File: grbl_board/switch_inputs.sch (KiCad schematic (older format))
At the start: 19 parts

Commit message: spindle control stage
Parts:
- added J?: PROBE, symbol Connector:Screw_Terminal_01x02
- added R?: 1k, symbol Device:R
- added U?: 6N137, Package_DIP:DIP-8_W7.62mm, symbol Isolator:6N137
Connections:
- net +12V: now also J?.1 (Pin_1)
- net +5V: now also U?.7 (EN), U?.8 (VCC)
- net GND: now also U?.3 (C), U?.5 (GND)
- new net: R?.1, U?.2 (A)
- new net: J?.2 (Pin_2), R?.2
- new net PROBE: U?.6 (VO)
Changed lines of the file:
@@
 Wire Wire Line
 	6600 5350 6900 5350
+$Comp
+L Isolator:6N137 U?
+U 1 1 6269851C
+P 3500 6900
+F 0 "U?" H 3500 7367 50  0000 C CNN
+F 1 "6N137" H 3500 7276 50  0000 C CNN
+F 2 "Package_DIP:DIP-8_W7.62mm" H 3500 6400 50  0001 C CNN
+F 3 "https://docs.broadcom.com/docs/AV02-0940EN" H 2650 7450 50  0001 C CNN
+	1    3500 6900
+	1    0    0    -1
+$EndComp
+$Comp
+L power:+5V #PWR?
+U 1 1 62698522
+P 4000 6500
+F 0 "#PWR?" H 4000 6350 50  0001 C CNN
+F 1 "+5V" H 4015 6673 50  0000 C CNN
+F 2 "" H 4000 6500 50  0001 C CNN
+F 3 "" H 4000 6500 50  0001 C CNN
+	1    4000 6500
+	1    0    0    -1
+$EndComp
+Wire Wire Line
+	4000 6500 4000 6700
+Wire Wire Line
+	4000 6700 3800 6700
+Wire Wire Line
+	4000 6700 4000 6800
+Wire Wire Line
+	4000 6800 3800 6800
+Connection ~ 4000 6700
+$Comp
+L power:GND #PWR?
+U 1 1 6269852D
+P 4000 7150
+F 0 "#PWR?" H 4000 6900 50  0001 C CNN
+F 1 "GND" H 4005 6977 50  0000 C CNN
+F 2 "" H 4000 7150 50  0001 C CNN
+F 3 "" H 4000 7150 50  0001 C CNN
+	1    4000 7150
+	1    0    0    -1
+$EndComp
+Wire Wire Line
+	4000 7150 4000 7100
+Wire Wire Line
+	4000 7100 3800 7100
+$Comp
+L Device:R R?
+U 1 1 62698535
+P 2750 6900
+F 0 "R?" V 2543 6900 50  0000 C CNN
+F 1 "1k" V 2634 6900 50  0000 C CNN
+F 2 "" V 2680 6900 50  0001 C CNN
+F 3 "~" H 2750 6900 50  0001 C CNN
+	1    2750 6900
+	0    1    1    0
+$EndComp
+$Comp
+L power:GND #PWR?
+U 1 1 6269853B
+P 3000 7150
+F 0 "#PWR?" H 3000 6900 50  0001 C CNN
+F 1 "GND" H 3005 6977 50  0000 C CNN
+F 2 "" H 3000 7150 50  0001 C CNN
+F 3 "" H 3000 7150 50  0001 C CNN
+	1    3000 7150
+	1    0    0    -1
+$EndComp
+Wire Wire Line
+	3200 7100 3000 7100
+Wire Wire Line
+	3000 7100 3000 7150
+Wire Wire Line
+	2900 6900 3200 6900
+Text HLabel 4000 6900 2    50   Input ~ 0
+PROBE
+Wire Wire Line
+	4000 6900 3800 6900
+$Comp
+L Connector:Screw_Terminal_01x02 J?
+U 1 1 62698546
+P 1400 7000
+F 0 "J?" H 1318 6675 50  0000 C CNN
+F 1 "PROBE" H 1318 6766 50  0000 C CNN
+F 2 "" H 1400 7000 50  0001 C CNN
+F 3 "~" H 1400 7000 50  0001 C CNN
+	1    1400 7000
+	-1   0    0    1
+$EndComp
+Wire Wire Line
+	1600 6900 2600 6900
+$Comp
+L power:+12V #PWR?
+U 1 1 6269854D
+P 1800 6700
+F 0 "#PWR?" H 1800 6550 50  0001 C CNN
+F 1 "+12V" H 1815 6873 50  0000 C CNN
+F 2 "" H 1800 6700 50  0001 C CNN
+F 3 "" H 1800 6700 50  0001 C CNN
+	1    1800 6700
+	1    0    0    -1
+$EndComp
+Wire Wire Line
+	1800 6700 1800 7000
+Wire Wire Line
+	1800 7000 1600 7000
 $EndSCHEMATC

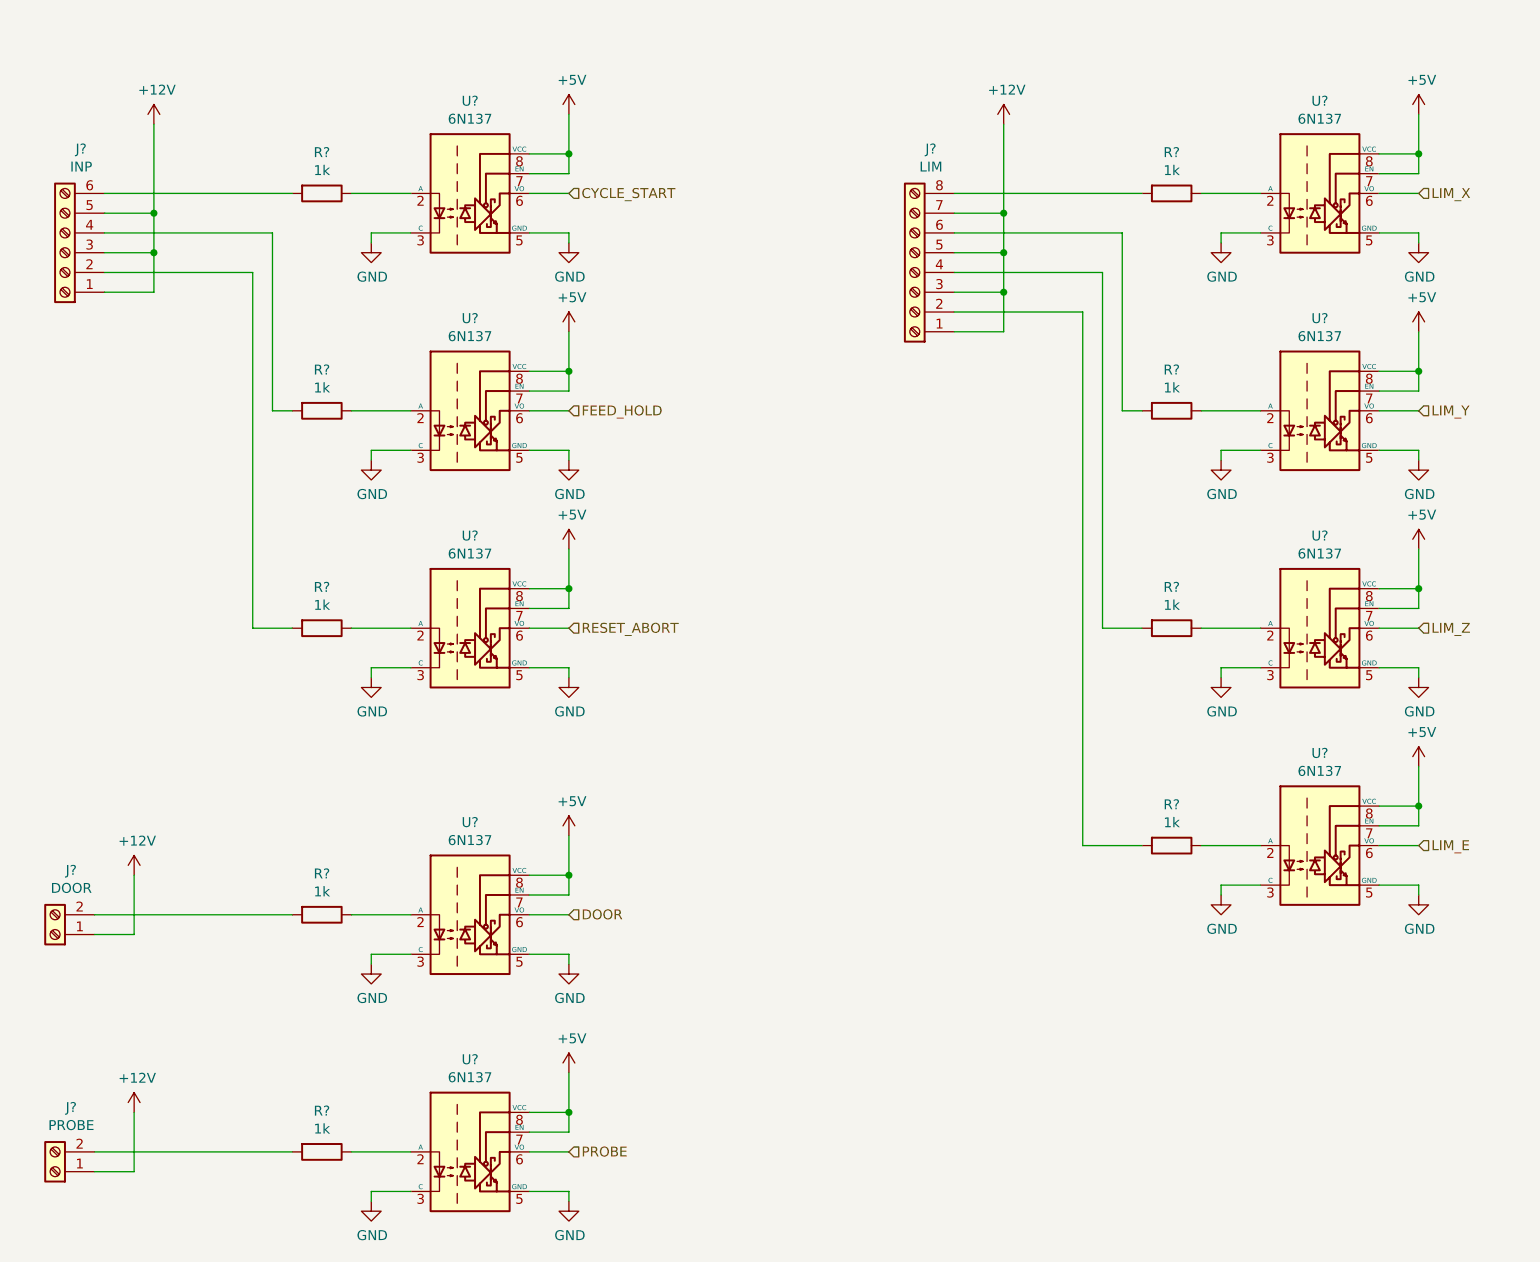
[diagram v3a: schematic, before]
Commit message: added some footprint associations
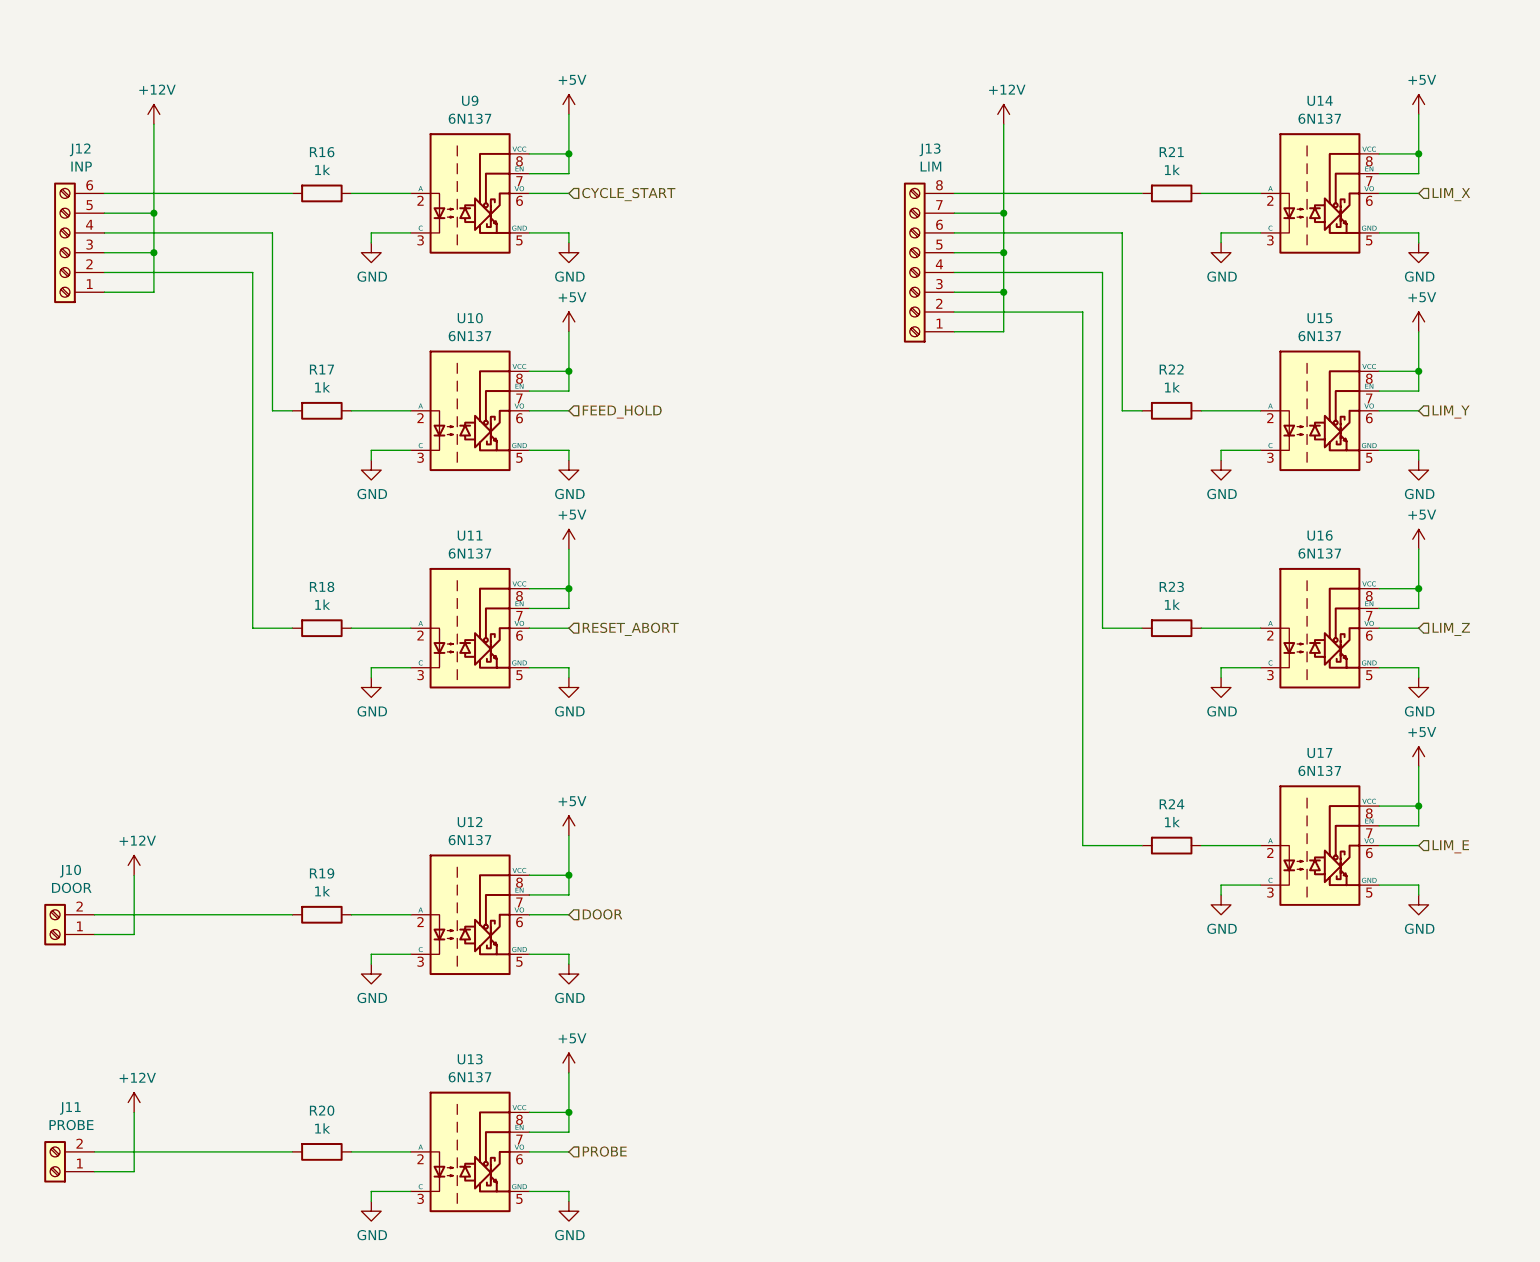
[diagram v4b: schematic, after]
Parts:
- J10, J11: renamed from J?; footprint (none) -> Connector_Phoenix_MC:PhoenixContact_MC_1,5_2-G-3.81_1x02_P3.81mm_Horizontal; Digikey Part No. (none) -> ED2808-ND
- J12: renamed from J?; footprint (none) -> Connector_Phoenix_MC:PhoenixContact_MC_1,5_6-G-3.81_1x06_P3.81mm_Horizontal; Digikey Part No. (none) -> ED2812-ND
- J13: renamed from J?; footprint (none) -> Connector_Phoenix_MC:PhoenixContact_MC_1,5_8-G-3.81_1x08_P3.81mm_Horizontal; Digikey Part No. (none) -> ED2814-ND
- R16, R17, R18, R19, R20, R21, R22, R23, R24: renamed from R?; footprint (none) -> Resistor_SMD:R_1206_3216Metric_Pad1.30x1.75mm_HandSolder; Digikey Part No. (none) -> 311-1.0KERCT-ND
- gave numbers to parts that had none: 9

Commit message: complete footprint associations
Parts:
- U10, U11, U12, U13, U14, U15, U16, U17, U9: Digikey Part No. (none) -> 6N137-X007TCT-ND
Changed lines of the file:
@@
 F 1 "6N137" H 3500 2426 50  0000 C CNN
 F 2 "Package_DIP:DIP-8_W7.62mm" H 3500 1550 50  0001 C CNN
-F 3 "https://docs.broadcom.com/docs/AV02-0940EN" H 2650 2600 50  0001 C CNN
+F 3 "https://www.vishay.com/docs/84732/6n137.pdf" H 2650 2600 50  0001 C CNN
+F 4 "6N137-X007TCT-ND" H 3500 2050 50  0001 C CNN "Digikey Part No."
 	1    3500 2050
 	1    0    0    -1
@@
 F 1 "6N137" H 3500 3526 50  0000 C CNN
 F 2 "Package_DIP:DIP-8_W7.62mm" H 3500 2650 50  0001 C CNN
-F 3 "https://docs.broadcom.com/docs/AV02-0940EN" H 2650 3700 50  0001 C CNN
+F 3 "https://www.vishay.com/docs/84732/6n137.pdf" H 2650 3700 50  0001 C CNN
+F 4 "6N137-X007TCT-ND" H 3500 3150 50  0001 C CNN "Digikey Part No."
 	1    3500 3150
 	1    0    0    -1
@@
 F 1 "6N137" H 3500 4626 50  0000 C CNN
 F 2 "Package_DIP:DIP-8_W7.62mm" H 3500 3750 50  0001 C CNN
-F 3 "https://docs.broadcom.com/docs/AV02-0940EN" H 2650 4800 50  0001 C CNN
+F 3 "https://www.vishay.com/docs/84732/6n137.pdf" H 2650 4800 50  0001 C CNN
+F 4 "6N137-X007TCT-ND" H 3500 4250 50  0001 C CNN "Digikey Part No."
 	1    3500 4250
 	1    0    0    -1
@@
 F 1 "6N137" H 3500 6076 50  0000 C CNN
 F 2 "Package_DIP:DIP-8_W7.62mm" H 3500 5200 50  0001 C CNN
-F 3 "https://docs.broadcom.com/docs/AV02-0940EN" H 2650 6250 50  0001 C CNN
+F 3 "https://www.vishay.com/docs/84732/6n137.pdf" H 2650 6250 50  0001 C CNN
+F 4 "6N137-X007TCT-ND" H 3500 5700 50  0001 C CNN "Digikey Part No."
 	1    3500 5700
 	1    0    0    -1
@@
 F 1 "6N137" H 7800 2426 50  0000 C CNN
 F 2 "Package_DIP:DIP-8_W7.62mm" H 7800 1550 50  0001 C CNN
-F 3 "https://docs.broadcom.com/docs/AV02-0940EN" H 6950 2600 50  0001 C CNN
+F 3 "https://www.vishay.com/docs/84732/6n137.pdf" H 6950 2600 50  0001 C CNN
+F 4 "6N137-X007TCT-ND" H 7800 2050 50  0001 C CNN "Digikey Part No."
 	1    7800 2050
 	1    0    0    -1
@@
 F 1 "6N137" H 7800 3526 50  0000 C CNN
 F 2 "Package_DIP:DIP-8_W7.62mm" H 7800 2650 50  0001 C CNN
-F 3 "https://docs.broadcom.com/docs/AV02-0940EN" H 6950 3700 50  0001 C CNN
+F 3 "https://www.vishay.com/docs/84732/6n137.pdf" H 6950 3700 50  0001 C CNN
+F 4 "6N137-X007TCT-ND" H 7800 3150 50  0001 C CNN "Digikey Part No."
 	1    7800 3150
 	1    0    0    -1
@@
 F 1 "6N137" H 7800 4626 50  0000 C CNN
 F 2 "Package_DIP:DIP-8_W7.62mm" H 7800 3750 50  0001 C CNN
-F 3 "https://docs.broadcom.com/docs/AV02-0940EN" H 6950 4800 50  0001 C CNN
+F 3 "https://www.vishay.com/docs/84732/6n137.pdf" H 6950 4800 50  0001 C CNN
+F 4 "6N137-X007TCT-ND" H 7800 4250 50  0001 C CNN "Digikey Part No."
 	1    7800 4250
 	1    0    0    -1
@@
 F 1 "6N137" H 7800 5726 50  0000 C CNN
 F 2 "Package_DIP:DIP-8_W7.62mm" H 7800 4850 50  0001 C CNN
-F 3 "https://docs.broadcom.com/docs/AV02-0940EN" H 6950 5900 50  0001 C CNN
+F 3 "https://www.vishay.com/docs/84732/6n137.pdf" H 6950 5900 50  0001 C CNN
+F 4 "6N137-X007TCT-ND" H 7800 5350 50  0001 C CNN "Digikey Part No."
 	1    7800 5350
 	1    0    0    -1
@@
 F 1 "6N137" H 3500 7276 50  0000 C CNN
 F 2 "Package_DIP:DIP-8_W7.62mm" H 3500 6400 50  0001 C CNN
-F 3 "https://docs.broadcom.com/docs/AV02-0940EN" H 2650 7450 50  0001 C CNN
+F 3 "https://www.vishay.com/docs/84732/6n137.pdf" H 2650 7450 50  0001 C CNN
+F 4 "6N137-X007TCT-ND" H 3500 6900 50  0001 C CNN "Digikey Part No."
 	1    3500 6900
 	1    0    0    -1

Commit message: fixed mismatch for 6n137
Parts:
- U10, U11, U12, U13, U14, U15, U16, U17, U9: footprint Package_DIP:DIP-8_W7.62mm -> Package_DIP:DIP-8_W7.62mm_Socket; Digikey Part No. 6N137-X007TCT-ND -> 6N137IS-ND
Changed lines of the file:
@@
 F 0 "U9" H 3500 2517 50  0000 C CNN
 F 1 "6N137" H 3500 2426 50  0000 C CNN
-F 2 "Package_DIP:DIP-8_W7.62mm" H 3500 1550 50  0001 C CNN
-F 3 "https://www.vishay.com/docs/84732/6n137.pdf" H 2650 2600 50  0001 C CNN
-F 4 "6N137-X007TCT-ND" H 3500 2050 50  0001 C CNN "Digikey Part No."
+F 2 "Package_DIP:DIP-8_W7.62mm_Socket" H 3500 1550 50  0001 C CNN
+F 3 "http://isocom.com/wp-content/uploads/2017/10/DD93209-6N137_ICPL2601_2611-280917.pdf" H 2650 2600 50  0001 C CNN
+F 4 "6N137IS-ND" H 3500 2050 50  0001 C CNN "Digikey Part No."
 	1    3500 2050
 	1    0    0    -1
@@
 F 0 "U10" H 3500 3617 50  0000 C CNN
 F 1 "6N137" H 3500 3526 50  0000 C CNN
-F 2 "Package_DIP:DIP-8_W7.62mm" H 3500 2650 50  0001 C CNN
-F 3 "https://www.vishay.com/docs/84732/6n137.pdf" H 2650 3700 50  0001 C CNN
-F 4 "6N137-X007TCT-ND" H 3500 3150 50  0001 C CNN "Digikey Part No."
+F 2 "Package_DIP:DIP-8_W7.62mm_Socket" H 3500 2650 50  0001 C CNN
+F 3 "http://isocom.com/wp-content/uploads/2017/10/DD93209-6N137_ICPL2601_2611-280917.pdf" H 2650 3700 50  0001 C CNN
+F 4 "6N137IS-ND" H 3500 3150 50  0001 C CNN "Digikey Part No."
 	1    3500 3150
 	1    0    0    -1
@@
 F 0 "U11" H 3500 4717 50  0000 C CNN
 F 1 "6N137" H 3500 4626 50  0000 C CNN
-F 2 "Package_DIP:DIP-8_W7.62mm" H 3500 3750 50  0001 C CNN
-F 3 "https://www.vishay.com/docs/84732/6n137.pdf" H 2650 4800 50  0001 C CNN
-F 4 "6N137-X007TCT-ND" H 3500 4250 50  0001 C CNN "Digikey Part No."
+F 2 "Package_DIP:DIP-8_W7.62mm_Socket" H 3500 3750 50  0001 C CNN
+F 3 "http://isocom.com/wp-content/uploads/2017/10/DD93209-6N137_ICPL2601_2611-280917.pdf" H 2650 4800 50  0001 C CNN
+F 4 "6N137IS-ND" H 3500 4250 50  0001 C CNN "Digikey Part No."
 	1    3500 4250
 	1    0    0    -1
@@
 F 0 "U12" H 3500 6167 50  0000 C CNN
 F 1 "6N137" H 3500 6076 50  0000 C CNN
-F 2 "Package_DIP:DIP-8_W7.62mm" H 3500 5200 50  0001 C CNN
-F 3 "https://www.vishay.com/docs/84732/6n137.pdf" H 2650 6250 50  0001 C CNN
-F 4 "6N137-X007TCT-ND" H 3500 5700 50  0001 C CNN "Digikey Part No."
+F 2 "Package_DIP:DIP-8_W7.62mm_Socket" H 3500 5200 50  0001 C CNN
+F 3 "http://isocom.com/wp-content/uploads/2017/10/DD93209-6N137_ICPL2601_2611-280917.pdf" H 2650 6250 50  0001 C CNN
+F 4 "6N137IS-ND" H 3500 5700 50  0001 C CNN "Digikey Part No."
 	1    3500 5700
 	1    0    0    -1
@@
 F 0 "U14" H 7800 2517 50  0000 C CNN
 F 1 "6N137" H 7800 2426 50  0000 C CNN
-F 2 "Package_DIP:DIP-8_W7.62mm" H 7800 1550 50  0001 C CNN
-F 3 "https://www.vishay.com/docs/84732/6n137.pdf" H 6950 2600 50  0001 C CNN
-F 4 "6N137-X007TCT-ND" H 7800 2050 50  0001 C CNN "Digikey Part No."
+F 2 "Package_DIP:DIP-8_W7.62mm_Socket" H 7800 1550 50  0001 C CNN
+F 3 "http://isocom.com/wp-content/uploads/2017/10/DD93209-6N137_ICPL2601_2611-280917.pdf" H 6950 2600 50  0001 C CNN
+F 4 "6N137IS-ND" H 7800 2050 50  0001 C CNN "Digikey Part No."
 	1    7800 2050
 	1    0    0    -1
@@
 F 0 "U15" H 7800 3617 50  0000 C CNN
 F 1 "6N137" H 7800 3526 50  0000 C CNN
-F 2 "Package_DIP:DIP-8_W7.62mm" H 7800 2650 50  0001 C CNN
-F 3 "https://www.vishay.com/docs/84732/6n137.pdf" H 6950 3700 50  0001 C CNN
-F 4 "6N137-X007TCT-ND" H 7800 3150 50  0001 C CNN "Digikey Part No."
+F 2 "Package_DIP:DIP-8_W7.62mm_Socket" H 7800 2650 50  0001 C CNN
+F 3 "http://isocom.com/wp-content/uploads/2017/10/DD93209-6N137_ICPL2601_2611-280917.pdf" H 6950 3700 50  0001 C CNN
+F 4 "6N137IS-ND" H 7800 3150 50  0001 C CNN "Digikey Part No."
 	1    7800 3150
 	1    0    0    -1
@@
 F 0 "U16" H 7800 4717 50  0000 C CNN
 F 1 "6N137" H 7800 4626 50  0000 C CNN
-F 2 "Package_DIP:DIP-8_W7.62mm" H 7800 3750 50  0001 C CNN
-F 3 "https://www.vishay.com/docs/84732/6n137.pdf" H 6950 4800 50  0001 C CNN
-F 4 "6N137-X007TCT-ND" H 7800 4250 50  0001 C CNN "Digikey Part No."
+F 2 "Package_DIP:DIP-8_W7.62mm_Socket" H 7800 3750 50  0001 C CNN
+F 3 "http://isocom.com/wp-content/uploads/2017/10/DD93209-6N137_ICPL2601_2611-280917.pdf" H 6950 4800 50  0001 C CNN
+F 4 "6N137IS-ND" H 7800 4250 50  0001 C CNN "Digikey Part No."
 	1    7800 4250
 	1    0    0    -1
@@
 F 0 "U17" H 7800 5817 50  0000 C CNN
 F 1 "6N137" H 7800 5726 50  0000 C CNN
-F 2 "Package_DIP:DIP-8_W7.62mm" H 7800 4850 50  0001 C CNN
-F 3 "https://www.vishay.com/docs/84732/6n137.pdf" H 6950 5900 50  0001 C CNN
-F 4 "6N137-X007TCT-ND" H 7800 5350 50  0001 C CNN "Digikey Part No."
+F 2 "Package_DIP:DIP-8_W7.62mm_Socket" H 7800 4850 50  0001 C CNN
+F 3 "http://isocom.com/wp-content/uploads/2017/10/DD93209-6N137_ICPL2601_2611-280917.pdf" H 6950 5900 50  0001 C CNN
+F 4 "6N137IS-ND" H 7800 5350 50  0001 C CNN "Digikey Part No."
 	1    7800 5350
 	1    0    0    -1
@@
 F 0 "U13" H 3500 7367 50  0000 C CNN
 F 1 "6N137" H 3500 7276 50  0000 C CNN
-F 2 "Package_DIP:DIP-8_W7.62mm" H 3500 6400 50  0001 C CNN
-F 3 "https://www.vishay.com/docs/84732/6n137.pdf" H 2650 7450 50  0001 C CNN
-F 4 "6N137-X007TCT-ND" H 3500 6900 50  0001 C CNN "Digikey Part No."
+F 2 "Package_DIP:DIP-8_W7.62mm_Socket" H 3500 6400 50  0001 C CNN
+F 3 "http://isocom.com/wp-content/uploads/2017/10/DD93209-6N137_ICPL2601_2611-280917.pdf" H 2650 7450 50  0001 C CNN
+F 4 "6N137IS-ND" H 3500 6900 50  0001 C CNN "Digikey Part No."
 	1    3500 6900
 	1    0    0    -1
